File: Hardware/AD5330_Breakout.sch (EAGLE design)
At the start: 9 parts, among them U1 AD5330

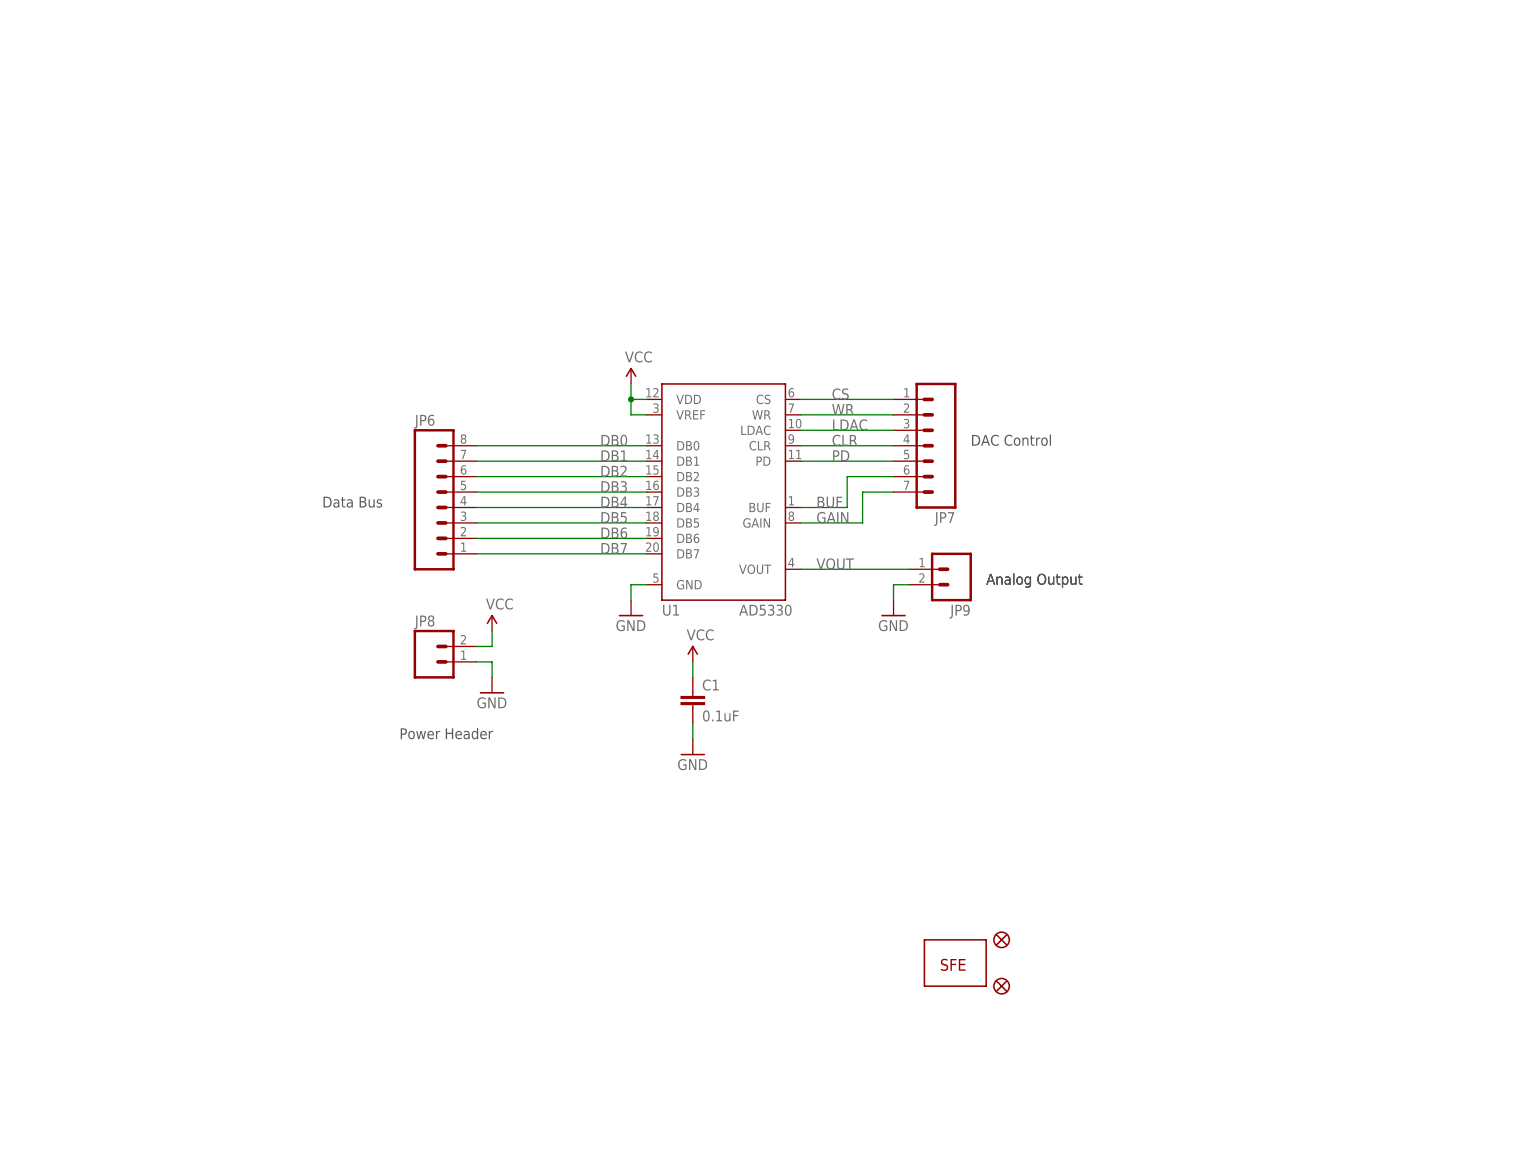
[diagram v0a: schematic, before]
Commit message: Revision changes
-Cleaned up schematic
-Added OSHW Logo
-0402->0603
-Added 10uf cap for filtration off of VDD as per the datasheet
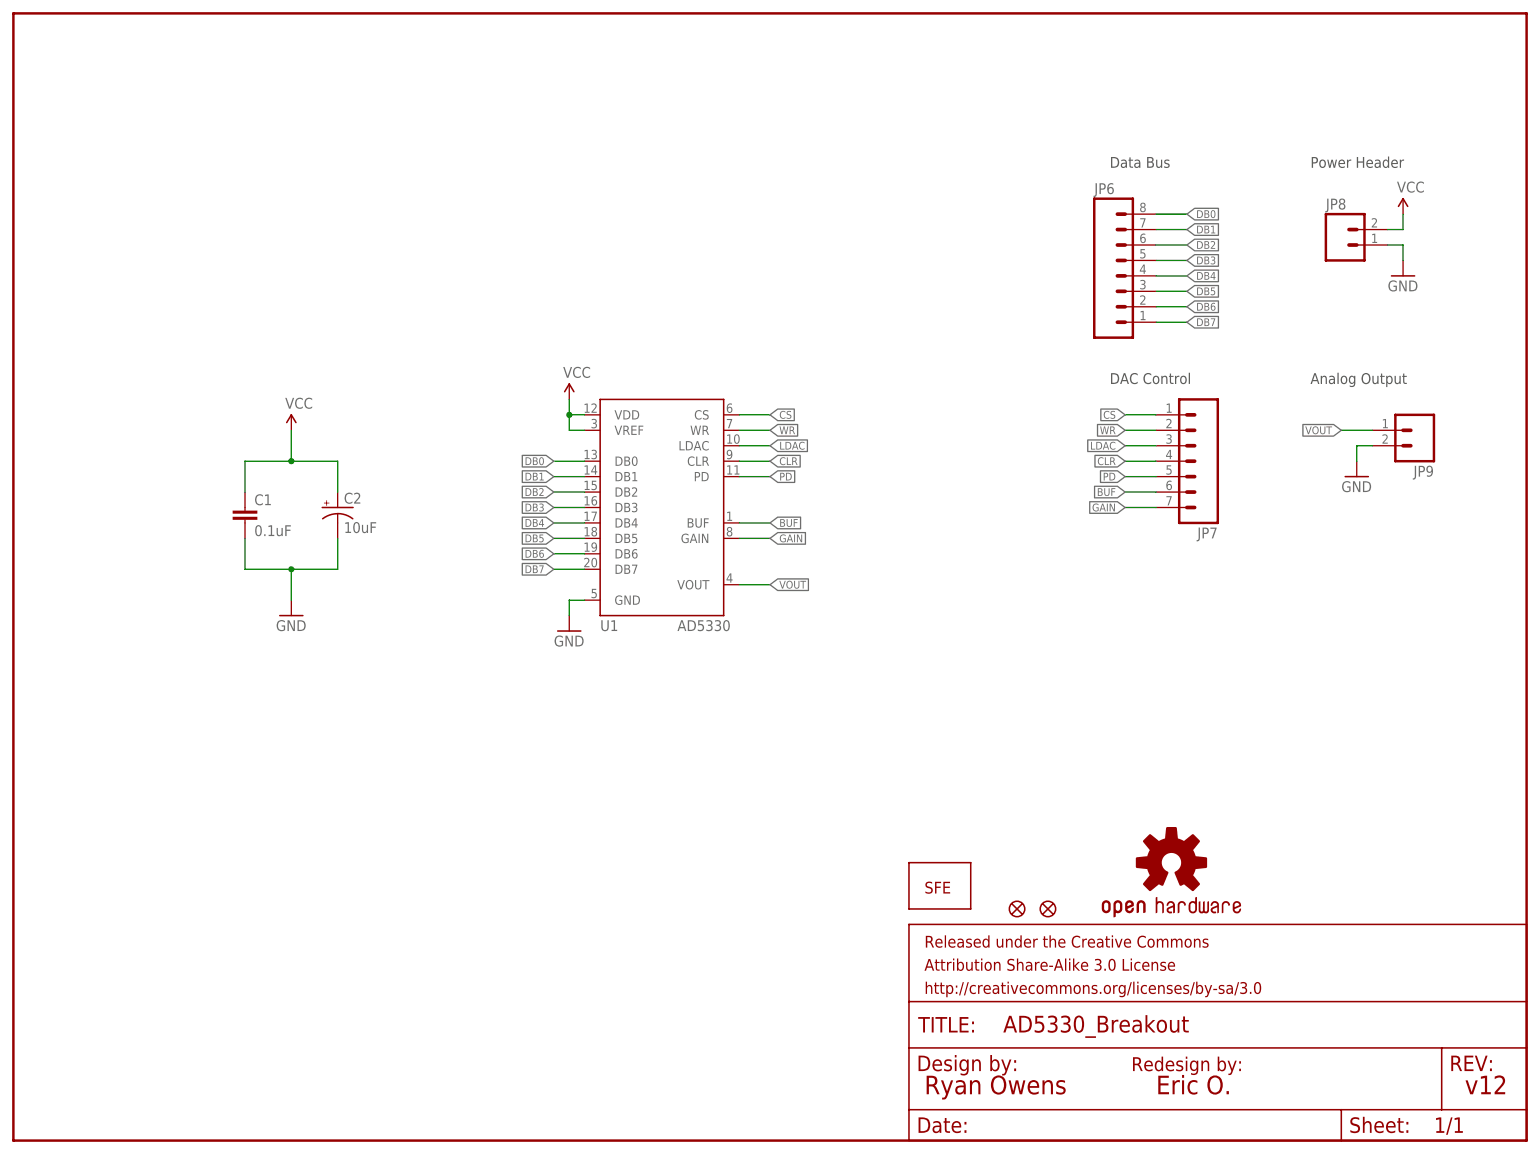
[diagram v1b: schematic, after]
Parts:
- added C2: 10uF, SparkFun-Capacitors:10UF-16V-10%(TANT)
- added FRAME1: FRAME-LETTER, SparkFun-Aesthetics:FRAME-LETTER
- added LOGO1: OSHW-LOGOS, SparkFun-Aesthetics:OSHW-LOGOS
- C1: device SparkFun:CAP0603-CAP -> SparkFun-Capacitors:0.1UF-25V(+80/-20%)(0603)
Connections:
- net GND: now also C2.-
- net VCC: now also C2.+
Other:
- note added: "Eric O."
- note added: "Redesign by:"
- note added: "Ryan Owens"
- note added: "v12"
- moved on the sheet: C1, JP6, JP7, JP8, JP9, U1

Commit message: Cleaned up schematic further
Grouped circuits together
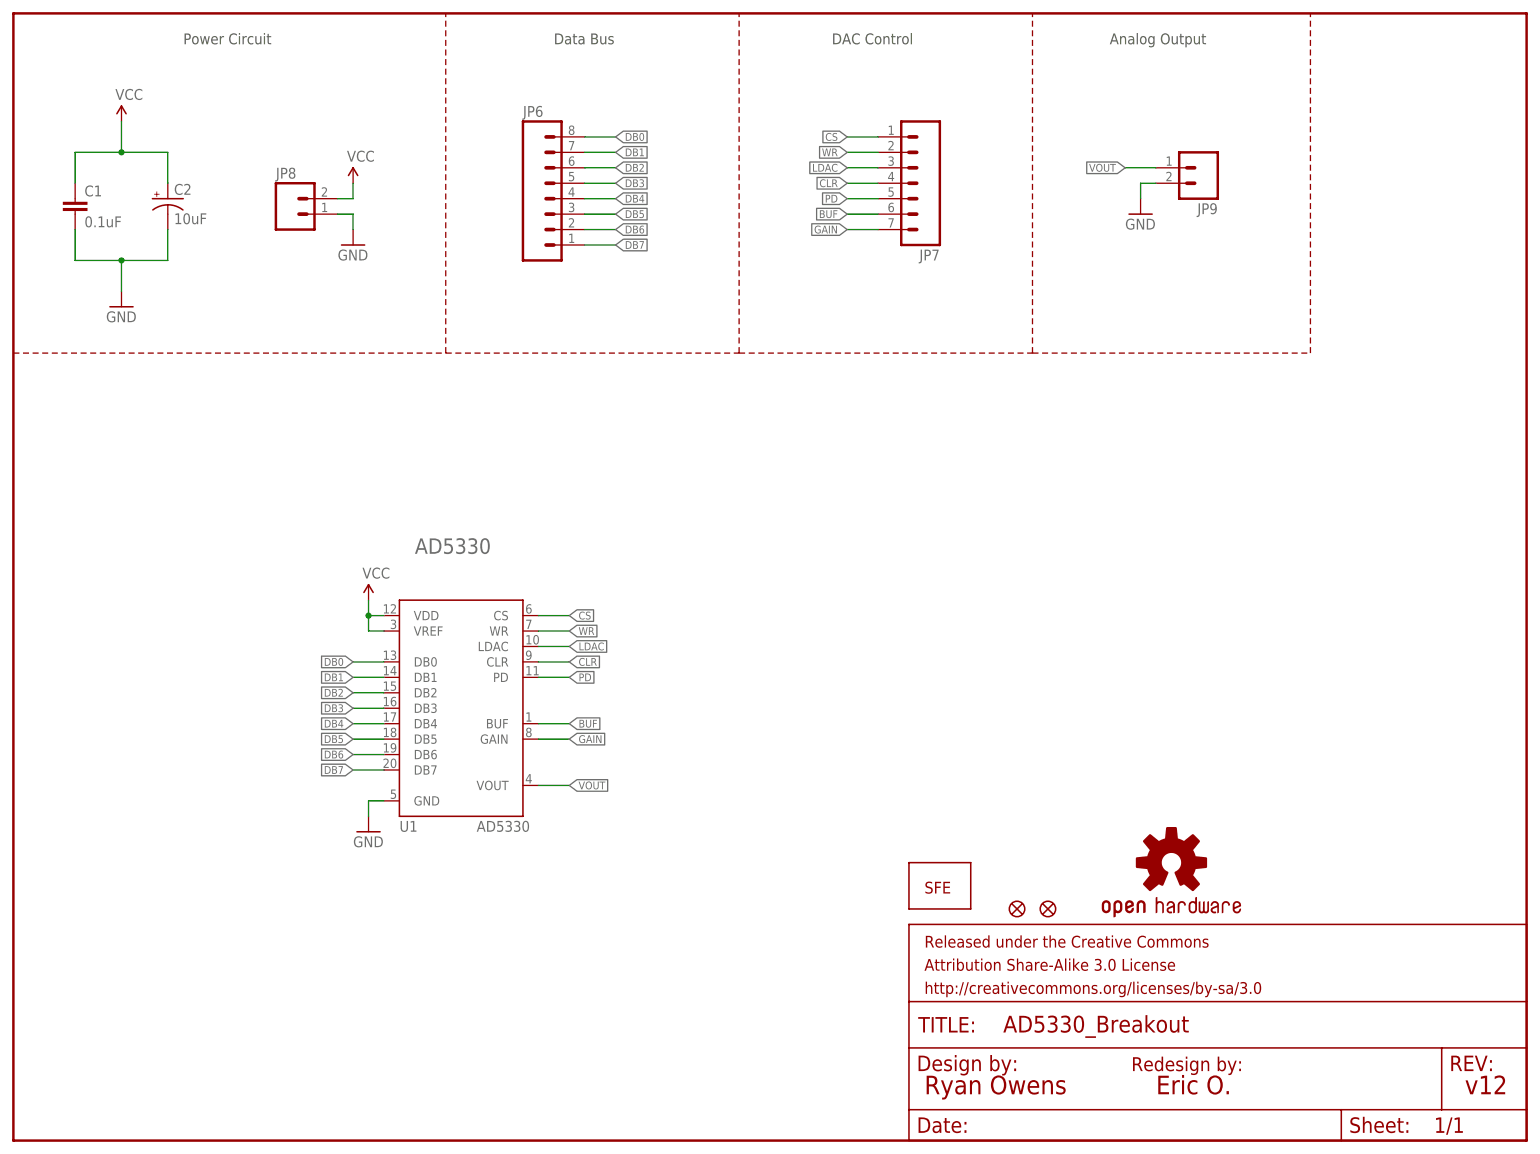
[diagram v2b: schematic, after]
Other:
- note added: "AD5330"
- note added: "Power Circuit"
- note removed: "Power Header"
- moved on the sheet: C1, C2, JP6, JP7, JP8, JP9, U1
